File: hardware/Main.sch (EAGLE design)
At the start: 90 parts, among them IC1 ESP32-WROOM-32D_M113DH3200PH3Q, IC2 LAN8720A-CP-ABC, IC3 R-78E5.0-1.0, IC4 LT1129MPST-3.3#PBF, J2 1727078, J3 HR911105A, J4 1727010, J5 1727049, J6 1727049, Q1 O50.0-JO32-B-3.3-1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

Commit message: Layout fertig
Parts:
- added C23: 100nF, rcl:C-EUC0603
- added IC5: 74LVT2244PW,118, SamacSys_Parts:74LVT2244PW,118
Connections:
- new net N$1: IC5.1Y0, R32.1
- new net N$10: IC5.1Y2, R36.1
- new net N$17: IC5.1Y3, R38.1
- new net N$32: IC5.2Y0, R4.1
- new net N$7: IC5.1Y1, R34.1
- net +5V: now also C23.1, IC5.VCC
- net GND: now also C23.2, IC5.!1OE, IC5.!2OE, IC5.2A1, IC5.2A2, IC5.2A3, IC5.GND
- net REL_CH_00: now also IC5.1A0; no longer R32.1
- net REL_CH_01: now also IC5.1A1; no longer R34.1
- net REL_CH_02: now also IC5.1A2; no longer R36.1
- net REL_CH_03: now also IC5.1A3; no longer R38.1
- net REL_CH_04: now also IC5.2A0; no longer R4.1
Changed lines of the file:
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@@
 <part name="GND46" library="supply1" library_urn="urn:adsk.eagle:library:371" deviceset="GND" device=""/>
 <part name="C22" library="rcl" library_urn="urn:adsk.eagle:library:334" deviceset="C-EU" device="C0603" package3d_urn="urn:adsk.eagle:package:23616/2" value="10U/6,3V"/>
+<part name="IC5" library="SamacSys_Parts" deviceset="74LVT2244PW,118" device=""/>
+<part name="GND47" library="supply1" library_urn="urn:adsk.eagle:library:371" deviceset="GND" device=""/>
+<part name="C23" library="rcl" library_urn="urn:adsk.eagle:library:334" deviceset="C-EU" device="C0603" package3d_urn="urn:adsk.eagle:package:23616/2" value="100nF"/>
+<part name="P+6" library="supply1" library_urn="urn:adsk.eagle:library:371" deviceset="+5V" device=""/>
+<part name="GND48" library="supply1" library_urn="urn:adsk.eagle:library:371" deviceset="GND" device=""/>
+<part name="GND49" library="supply1" library_urn="urn:adsk.eagle:library:371" deviceset="GND" device=""/>
 </parts>
 <sheets>
@@
 <attribute name="VALUE" x="271.78" y="214.63" size="1.778" layer="96" align="center-left"/>
 </instance>
+<instance part="IC5" gate="G$1" x="67.31" y="160.02" smashed="yes">
+<attribute name="NAME" x="91.44" y="167.64" size="1.778" layer="95" align="center-left"/>
+<attribute name="VALUE" x="91.44" y="165.1" size="1.778" layer="96" align="center-left"/>
+</instance>
+<instance part="GND47" gate="1" x="44.45" y="165.1" smashed="yes">
+<attribute name="VALUE" x="41.91" y="162.56" size="1.778" layer="96"/>
+</instance>
+<instance part="C23" gate="G$1" x="44.45" y="175.26" smashed="yes">
+<attribute name="NAME" x="45.974" y="175.641" size="1.778" layer="95"/>
+<attribute name="VALUE" x="45.974" y="170.561" size="1.778" layer="96"/>
+</instance>
+<instance part="P+6" gate="1" x="35.56" y="181.61" smashed="yes" rot="R90">
+<attribute name="VALUE" x="40.64" y="179.07" size="1.778" layer="96" rot="R180"/>
+</instance>
+<instance part="GND48" gate="1" x="62.23" y="128.27" smashed="yes">
+<attribute name="VALUE" x="59.69" y="125.73" size="1.778" layer="96"/>
+</instance>
+<instance part="GND49" gate="1" x="97.79" y="128.27" smashed="yes">
+<attribute name="VALUE" x="95.25" y="125.73" size="1.778" layer="96"/>
+</instance>
 </instances>
 <busses>
@@
 <pinref part="R5" gate="G$1" pin="1"/>
 <wire x1="161.29" y1="20.32" x2="161.29" y2="25.4" width="0.1524" layer="91"/>
+</segment>
+<segment>
+<pinref part="GND47" gate="1" pin="GND"/>
+<pinref part="C23" gate="G$1" pin="2"/>
+<wire x1="44.45" y1="167.64" x2="44.45" y2="170.18" width="0.1524" layer="91"/>
+</segment>
+<segment>
+<pinref part="IC5" gate="G$1" pin="GND"/>
+<wire x1="67.31" y1="137.16" x2="62.23" y2="137.16" width="0.1524" layer="91"/>
+<wire x1="62.23" y1="137.16" x2="62.23" y2="130.81" width="0.1524" layer="91"/>
+<pinref part="IC5" gate="G$1" pin="!1OE"/>
+<wire x1="67.31" y1="160.02" x2="62.23" y2="160.02" width="0.1524" layer="91"/>
+<wire x1="62.23" y1="160.02" x2="62.23" y2="137.16" width="0.1524" layer="91"/>
+<junction x="62.23" y="137.16"/>
+<pinref part="GND48" gate="1" pin="GND"/>
+</segment>
+<segment>
+<pinref part="IC5" gate="G$1" pin="2A1"/>
+<wire x1="95.25" y1="142.24" x2="97.79" y2="142.24" width="0.1524" layer="91"/>
+<wire x1="97.79" y1="142.24" x2="97.79" y2="130.81" width="0.1524" layer="91"/>
+<pinref part="IC5" gate="G$1" pin="!2OE"/>
+<wire x1="95.25" y1="157.48" x2="97.79" y2="157.48" width="0.1524" layer="91"/>
+<wire x1="97.79" y1="157.48" x2="97.79" y2="152.4" width="0.1524" layer="91"/>
+<junction x="97.79" y="142.24"/>
+<pinref part="IC5" gate="G$1" pin="2A3"/>
+<wire x1="97.79" y1="152.4" x2="97.79" y2="147.32" width="0.1524" layer="91"/>
+<wire x1="97.79" y1="146.05" x2="97.79" y2="142.24" width="0.1524" layer="91"/>
+<wire x1="95.25" y1="152.4" x2="97.79" y2="152.4" width="0.1524" layer="91"/>
+<junction x="97.79" y="152.4"/>
+<pinref part="IC5" gate="G$1" pin="2A2"/>
+<wire x1="95.25" y1="147.32" x2="97.79" y2="147.32" width="0.1524" layer="91"/>
+<wire x1="97.79" y1="147.32" x2="97.79" y2="146.05" width="0.1524" layer="91"/>
+<pinref part="GND49" gate="1" pin="GND"/>
 </segment>
 </net>
@@
 </segment>
 </net>
-<net name="REL_CH_00" class="0">
-<segment>
-<pinref part="R32" gate="G$1" pin="1"/>
-<wire x1="143.51" y1="219.71" x2="127" y2="219.71" width="0.1524" layer="91"/>
-<label x="128.27" y="219.71" size="1.778" layer="95"/>
-</segment>
-</net>
 <net name="N$15" class="0">
 <segment>
@@
 <net name="REL_CH_01" class="0">
 <segment>
-<pinref part="R34" gate="G$1" pin="1"/>
-<wire x1="143.51" y1="172.72" x2="127" y2="172.72" width="0.1524" layer="91"/>
-<label x="128.27" y="172.72" size="1.778" layer="95"/>
+<label x="50.8" y="152.4" size="1.778" layer="95"/>
+<wire x1="67.31" y1="152.4" x2="50.8" y2="152.4" width="0.1524" layer="91"/>
+<pinref part="IC5" gate="G$1" pin="1A1"/>
 </segment>
 </net>
@@
 <net name="REL_CH_02" class="0">
 <segment>
-<pinref part="R36" gate="G$1" pin="1"/>
-<wire x1="143.51" y1="128.27" x2="127" y2="128.27" width="0.1524" layer="91"/>
-<label x="129.54" y="128.27" size="1.778" layer="95"/>
+<label x="50.8" y="147.32" size="1.778" layer="95"/>
+<wire x1="67.31" y1="147.32" x2="50.8" y2="147.32" width="0.1524" layer="91"/>
+<pinref part="IC5" gate="G$1" pin="1A2"/>
 </segment>
 </net>
@@
 <net name="REL_CH_03" class="0">
 <segment>
-<pinref part="R38" gate="G$1" pin="1"/>
-<wire x1="143.51" y1="80.01" x2="127" y2="80.01" width="0.1524" layer="91"/>
-<label x="128.27" y="80.01" size="1.778" layer="95"/>
+<label x="50.8" y="142.24" size="1.778" layer="95"/>
+<wire x1="67.31" y1="142.24" x2="50.8" y2="142.24" width="0.1524" layer="91"/>
+<pinref part="IC5" gate="G$1" pin="1A3"/>
 </segment>
 </net>
@@
 </segment>
 </net>
+<net name="+5V" class="0">
+<segment>
+<pinref part="C23" gate="G$1" pin="1"/>
+<wire x1="44.45" y1="177.8" x2="44.45" y2="181.61" width="0.1524" layer="91"/>
+<pinref part="P+6" gate="1" pin="+5V"/>
+<wire x1="38.1" y1="181.61" x2="44.45" y2="181.61" width="0.1524" layer="91"/>
+<junction x="44.45" y="181.61"/>
+<pinref part="IC5" gate="G$1" pin="VCC"/>
+<wire x1="95.25" y1="160.02" x2="101.6" y2="160.02" width="0.1524" layer="91"/>
+<wire x1="101.6" y1="160.02" x2="101.6" y2="181.61" width="0.1524" layer="91"/>
+<wire x1="101.6" y1="181.61" x2="44.45" y2="181.61" width="0.1524" layer="91"/>
+</segment>
+</net>
+<net name="REL_CH_00" class="0">
+<segment>
+<wire x1="67.31" y1="157.48" x2="50.8" y2="157.48" width="0.1524" layer="91"/>
+<label x="50.8" y="157.48" size="1.778" layer="95"/>
+<pinref part="IC5" gate="G$1" pin="1A0"/>
+</segment>
+</net>
+<net name="N$1" class="0">
+<segment>
+<pinref part="IC5" gate="G$1" pin="1Y0"/>
+<wire x1="95.25" y1="154.94" x2="124.46" y2="154.94" width="0.1524" layer="91"/>
+<pinref part="R32" gate="G$1" pin="1"/>
+<wire x1="124.46" y1="154.94" x2="124.46" y2="219.71" width="0.1524" layer="91"/>
+<wire x1="124.46" y1="219.71" x2="143.51" y2="219.71" width="0.1524" layer="91"/>
+</segment>
+</net>
+<net name="N$7" class="0">
+<segment>
+<pinref part="IC5" gate="G$1" pin="1Y1"/>
+<wire x1="95.25" y1="149.86" x2="128.27" y2="149.86" width="0.1524" layer="91"/>
+<pinref part="R34" gate="G$1" pin="1"/>
+<wire x1="128.27" y1="149.86" x2="128.27" y2="172.72" width="0.1524" layer="91"/>
+<wire x1="128.27" y1="172.72" x2="143.51" y2="172.72" width="0.1524" layer="91"/>
+</segment>
+</net>
+<net name="N$10" class="0">
+<segment>
+<pinref part="IC5" gate="G$1" pin="1Y2"/>
+<wire x1="95.25" y1="144.78" x2="128.27" y2="144.78" width="0.1524" layer="91"/>
+<pinref part="R36" gate="G$1" pin="1"/>
+<wire x1="128.27" y1="144.78" x2="128.27" y2="128.27" width="0.1524" layer="91"/>
+<wire x1="128.27" y1="128.27" x2="143.51" y2="128.27" width="0.1524" layer="91"/>
+</segment>
+</net>
+<net name="N$17" class="0">
+<segment>
+<pinref part="IC5" gate="G$1" pin="1Y3"/>
+<wire x1="95.25" y1="139.7" x2="124.46" y2="139.7" width="0.1524" layer="91"/>
+<wire x1="124.46" y1="139.7" x2="124.46" y2="80.01" width="0.1524" layer="91"/>
+<pinref part="R38" gate="G$1" pin="1"/>
+<wire x1="124.46" y1="80.01" x2="143.51" y2="80.01" width="0.1524" layer="91"/>
+</segment>
+</net>
+<net name="N$32" class="0">
+<segment>
+<pinref part="IC5" gate="G$1" pin="2Y0"/>
+<wire x1="67.31" y1="139.7" x2="57.15" y2="139.7" width="0.1524" layer="91"/>
+<wire x1="57.15" y1="139.7" x2="57.15" y2="38.1" width="0.1524" layer="91"/>
+<wire x1="57.15" y1="38.1" x2="143.51" y2="38.1" width="0.1524" layer="91"/>
+<pinref part="R4" gate="G$1" pin="1"/>
+</segment>
+</net>
 <net name="REL_CH_04" class="0">
 <segment>
-<pinref part="R4" gate="G$1" pin="1"/>
-<wire x1="143.51" y1="38.1" x2="127" y2="38.1" width="0.1524" layer="91"/>
-<label x="128.27" y="38.1" size="1.778" layer="95"/>
-</segment>
-</net>
+<wire x1="111.76" y1="137.16" x2="95.25" y2="137.16" width="0.1524" layer="91"/>
+<label x="99.06" y="137.16" size="1.778" layer="95"/>
+<pinref part="IC5" gate="G$1" pin="2A0"/>
+</segment>
+</net>

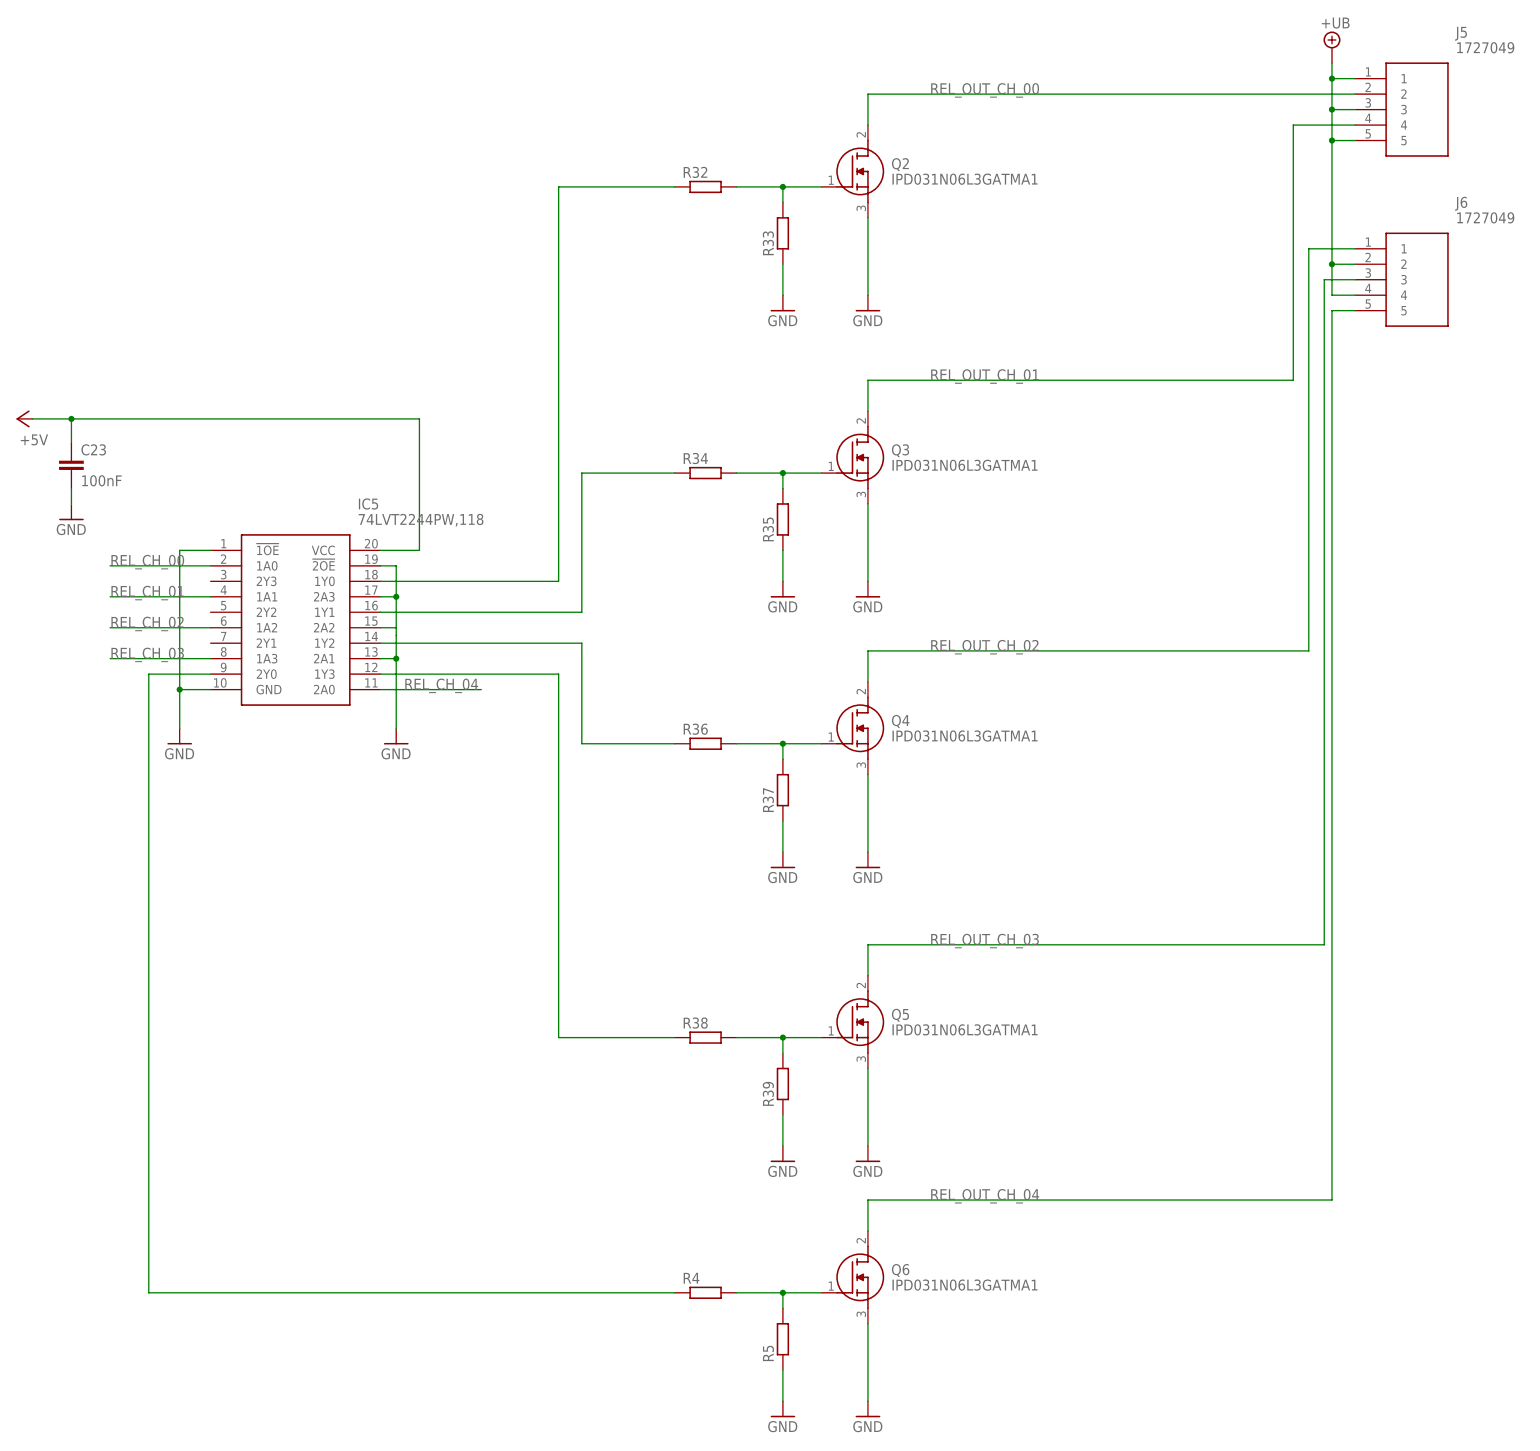
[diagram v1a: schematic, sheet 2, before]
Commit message: 1-gater ic statt 6 fach Treiber
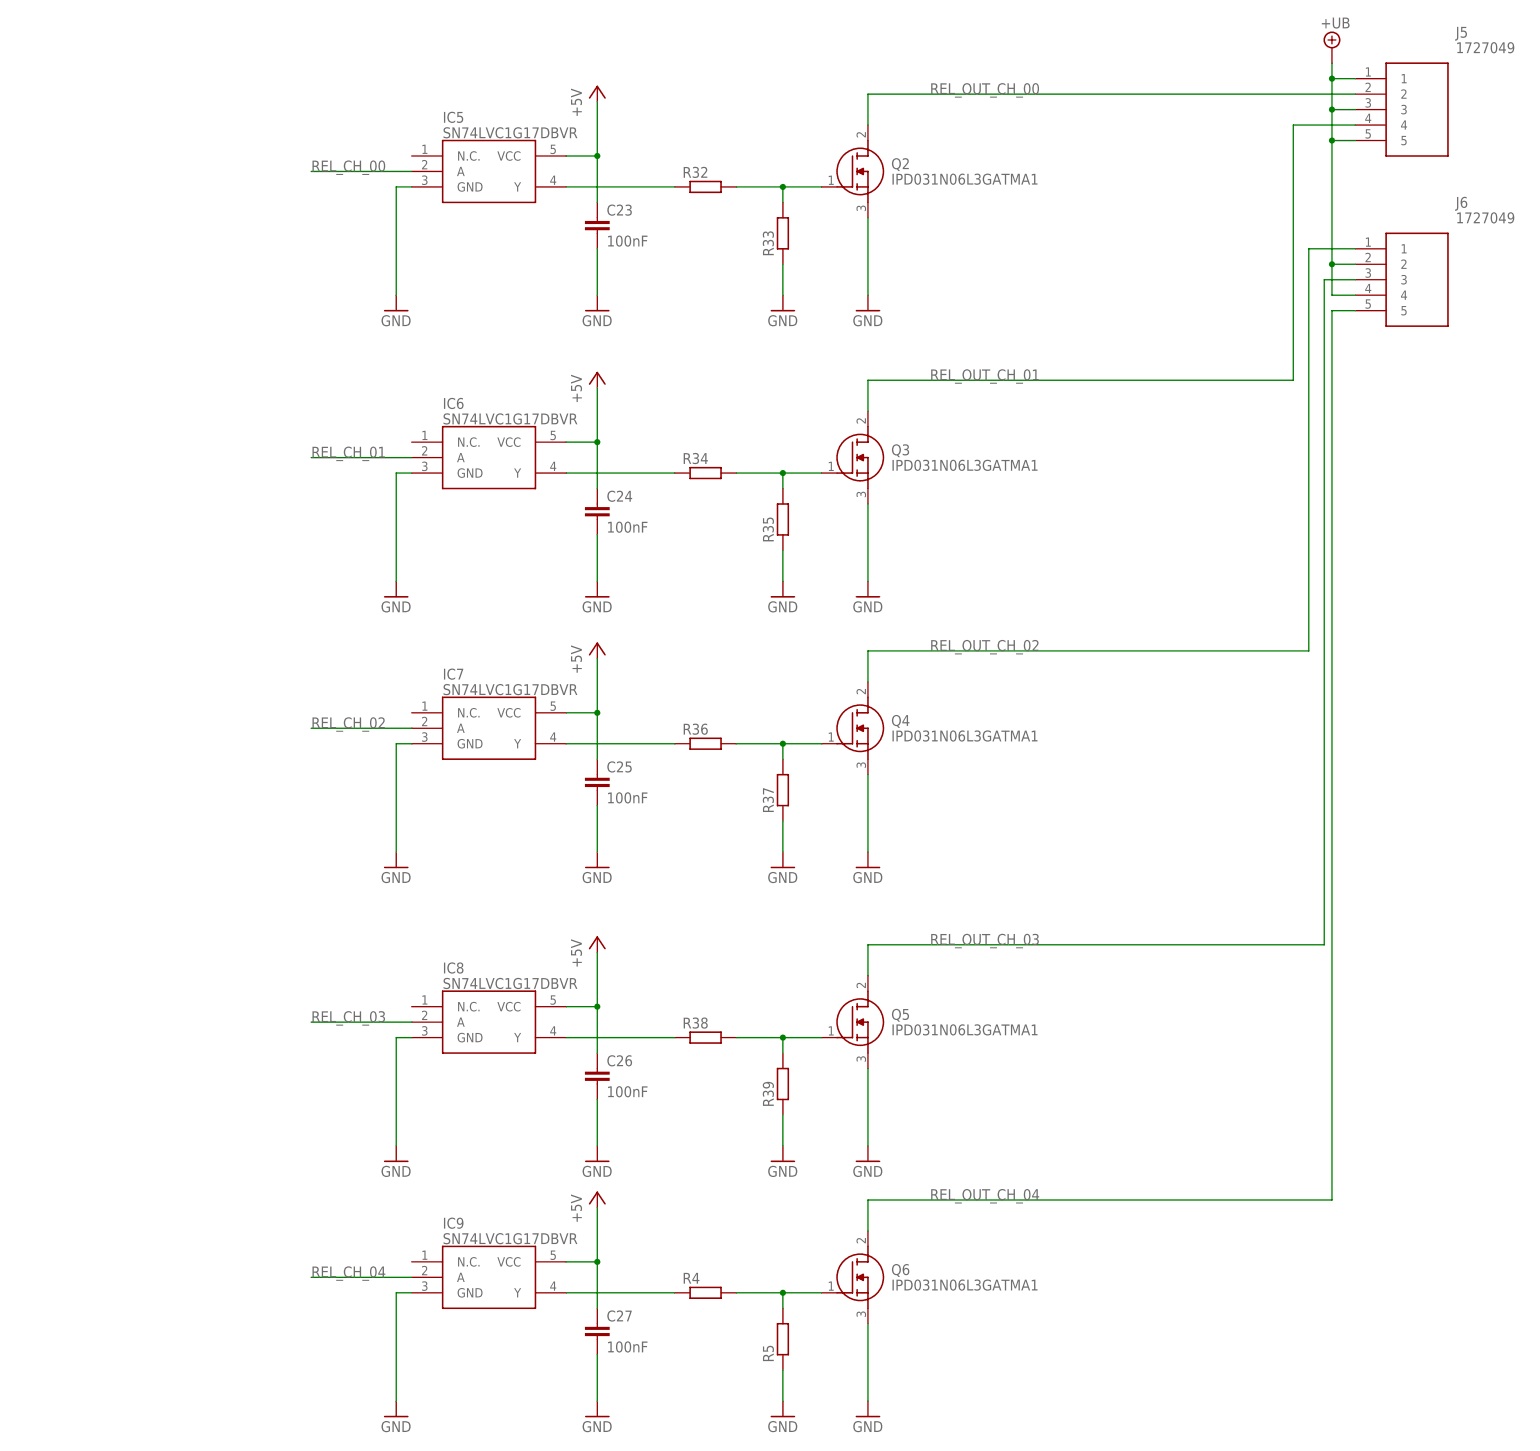
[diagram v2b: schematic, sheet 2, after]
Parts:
- added C24, C25, C26, C27: 100nF, rcl:C-EUC0603
- added IC6, IC7, IC8, IC9: SN74LVC1G17DBVR, SamacSys_Parts:SN74LVC1G17DBVR
- IC5: value 74LVT2244PW,118 -> SN74LVC1G17DBVR; device SamacSys_Parts:74LVT2244PW,118 -> SamacSys_Parts:SN74LVC1G17DBVR
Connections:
- net +5V: now also C24.1, C25.1, C26.1, C27.1, IC6.VCC, IC7.VCC, IC8.VCC, IC9.VCC
- net GND: now also C24.2, C25.2, C26.2, C27.2, IC6.GND, IC7.GND, IC8.GND, IC9.GND; no longer IC5.!1OE, IC5.!2OE, IC5.2A1, IC5.2A2, IC5.2A3
- net N$1: now also IC5.Y; no longer IC5.1Y0
- net N$10: now also IC7.Y; no longer IC5.1Y2
- net N$17: now also IC8.Y; no longer IC5.1Y3
- net N$32: now also IC9.Y; no longer IC5.2Y0
- net N$7: now also IC6.Y; no longer IC5.1Y1
- net REL_CH_00: now also IC5.A; no longer IC5.1A0
- net REL_CH_01: now also IC6.A; no longer IC5.1A1
- net REL_CH_02: now also IC7.A; no longer IC5.1A2
- net REL_CH_03: now also IC8.A; no longer IC5.1A3
- net REL_CH_04: now also IC9.A; no longer IC5.2A0
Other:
- moved on the sheet: C23
